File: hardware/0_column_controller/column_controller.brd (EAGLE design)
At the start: 45 parts, among them J3 RJ45, J4 JTAG, J7 RJ45, U1 PCA9615

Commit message: proto schematic for v11 column controller
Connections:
- new net RXI: U$13.PA11
- new net TXO: U$13.PA10
- net 5V: now also J3.4, J7.4
- net GND: now also J3.5, J7.5
- net LED0: now also U$13.PA02; no longer U$13.PA10
- net LED1: now also U$13.PA04; no longer U$13.PA11
- net LED2: now also U$13.PA06; no longer U$13.PA14
- net LED3: now also U$13.PA07; no longer U$13.PA15
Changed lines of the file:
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@@
 <contactref element="J1" pad="2"/>
 <contactref element="J1" pad="1"/>
+<contactref element="J3" pad="5"/>
+<contactref element="J7" pad="5"/>
+<wire x1="113.03" y1="106.045" x2="115.57" y2="104.775" width="0" layer="19" extent="1-1"/>
 <wire x1="109.22" y1="102.235" x2="113.03" y2="106.045" width="0" layer="19" extent="1-1"/>
-<wire x1="83.4" y1="106.68" x2="109.22" y2="102.235" width="0" layer="19" extent="1-1"/>
+<wire x1="106.68" y1="103.505" x2="109.22" y2="102.235" width="0" layer="19" extent="1-1"/>
+<wire x1="83.4" y1="106.68" x2="106.68" y2="103.505" width="0" layer="19" extent="1-1"/>
 <wire x1="83.4" y1="107.95" x2="83.4" y2="106.68" width="0" layer="19" extent="1-1"/>
 <wire x1="83.4" y1="109.22" x2="83.4" y2="107.95" width="0" layer="19" extent="1-1"/>
@@
 <contactref element="J1" pad="3"/>
 <contactref element="J1" pad="4"/>
-<wire x1="106.68" y1="106.045" x2="115.57" y2="102.235" width="0" layer="19" extent="1-1"/>
+<contactref element="J3" pad="4"/>
+<contactref element="J7" pad="4"/>
+<wire x1="113.03" y1="103.505" x2="115.57" y2="102.235" width="0" layer="19" extent="1-1"/>
+<wire x1="109.22" y1="104.775" x2="113.03" y2="103.505" width="0" layer="19" extent="1-1"/>
+<wire x1="106.68" y1="106.045" x2="109.22" y2="104.775" width="0" layer="19" extent="1-1"/>
 <wire x1="114.085" y1="72.7075" x2="115.57" y2="102.235" width="0" layer="19" extent="1-1"/>
 <wire x1="114.085" y1="71.12" x2="114.085" y2="72.7075" width="0" layer="19" extent="1-1"/>
@@
 <signal name="LED0">
 <contactref element="R6" pad="1"/>
-<contactref element="U$13" pad="PA10"/>
-<wire x1="21.59" y1="106.68" x2="105.83" y2="59.69" width="0" layer="19" extent="1-1"/>
+<contactref element="U$13" pad="PA02"/>
+<wire x1="36.83" y1="88.9" x2="105.83" y2="59.69" width="0" layer="19" extent="1-1"/>
 </signal>
 <signal name="LED1">
 <contactref element="R7" pad="1"/>
-<contactref element="U$13" pad="PA11"/>
-<wire x1="21.59" y1="104.14" x2="105.83" y2="58.42" width="0" layer="19" extent="1-1"/>
+<contactref element="U$13" pad="PA04"/>
+<wire x1="36.83" y1="96.52" x2="105.83" y2="58.42" width="0" layer="19" extent="1-1"/>
 </signal>
 <signal name="LED2">
 <contactref element="R8" pad="1"/>
-<contactref element="U$13" pad="PA14"/>
-<wire x1="21.59" y1="96.52" x2="105.83" y2="57.15" width="0" layer="19" extent="1-1"/>
+<contactref element="U$13" pad="PA06"/>
+<wire x1="21.59" y1="81.28" x2="105.83" y2="57.15" width="0" layer="19" extent="1-1"/>
 </signal>
 <signal name="LED3">
 <contactref element="R9" pad="1"/>
-<contactref element="U$13" pad="PA15"/>
-<wire x1="21.59" y1="88.9" x2="105.83" y2="55.88" width="0" layer="19" extent="1-1"/>
+<contactref element="U$13" pad="PA07"/>
+<wire x1="21.59" y1="78.74" x2="105.83" y2="55.88" width="0" layer="19" extent="1-1"/>
 </signal>
 <signal name="B0">
@@
 <wire x1="41.0972" y1="93.98" x2="36.83" y2="93.98" width="0" layer="19" extent="1-1"/>
 </signal>
+<signal name="TXO">
+<contactref element="U$13" pad="PA10"/>
+</signal>
+<signal name="RXI">
+<contactref element="U$13" pad="PA11"/>
+</signal>
 </signals>

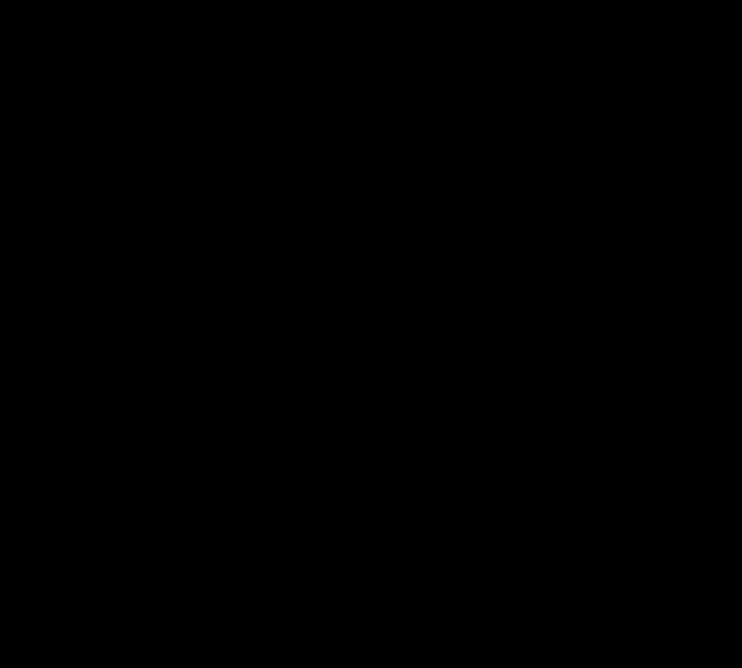
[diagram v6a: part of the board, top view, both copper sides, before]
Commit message: add uart / i2c / column debug access headers
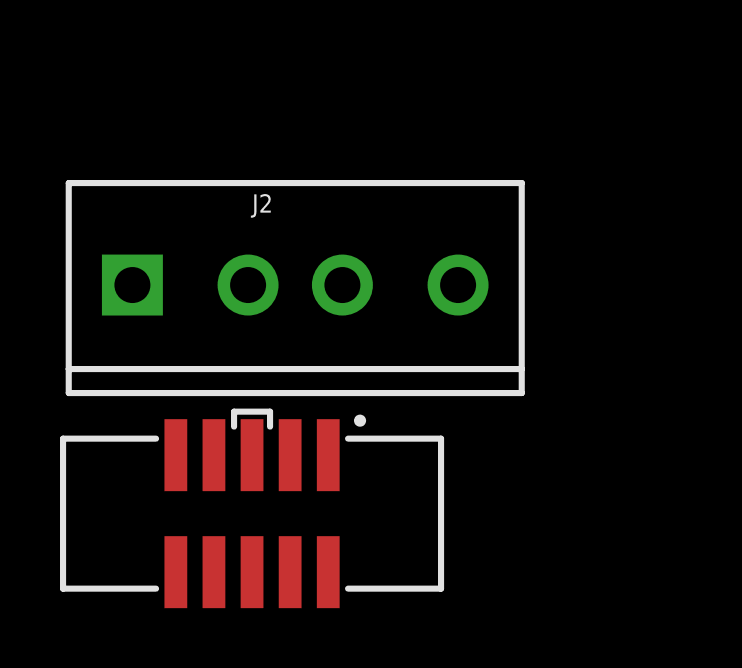
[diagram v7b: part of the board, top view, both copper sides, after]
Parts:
- added J2: (no value), SparkFun-Connectors:SCREWTERMINAL-3.5MM-4_LOCK
- added J5: JTAG, SparkFun-Connectors:2X5-SMD-1.27MM
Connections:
- net 5V: now also J5.4, J5.5, J5.7, J5.9
- net DOUT: now also J5.6
- net GND: now also J5.1, J5.2, J5.3
- net RXI: now also J2.4
- net SCL_COLUMN: now also J5.10
- net SCL_NETWORK: now also J2.1
- net SDA_COLUMN: now also J5.8
- net SDA_NETWORK: now also J2.2
- net TXO: now also J2.3
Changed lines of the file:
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@@
 <attribute name="VALUE" x="41.5036" y="92.837" size="0.6096" layer="27" font="vector" ratio="20" align="top-center"/>
+</element>
+<element name="J2" library="SparkFun-Connectors" package="SCREWTERMINAL-3.5MM-4_LOCK" value="" x="-5.08" y="-15.24">
+<attribute name="NAME" x="-1.27" y="-12.827" size="0.6096" layer="25" font="vector" ratio="20"/>
+<attribute name="VALUE" x="-1.27" y="-13.716" size="0.6096" layer="27" font="vector" ratio="20"/>
+</element>
+<element name="J5" library="SparkFun-Connectors" package="2X5-SMD-1.27MM" value="JTAG" x="-1.27" y="-22.86">
+<attribute name="PROD_ID" value="CONN-14503" x="-1.27" y="-22.86" size="1.778" layer="27" font="vector" ratio="15" display="off"/>
 </element>
 </elements>
@@
 <contactref element="J3" pad="5"/>
 <contactref element="J7" pad="5"/>
+<contactref element="J5" pad="1"/>
+<contactref element="J5" pad="3"/>
+<contactref element="J5" pad="2"/>
 <wire x1="113.03" y1="106.045" x2="115.57" y2="104.775" width="0" layer="19" extent="1-1"/>
 <wire x1="109.22" y1="102.235" x2="113.03" y2="106.045" width="0" layer="19" extent="1-1"/>
@@
 <wire x1="36.83" y1="104.14" x2="79.021" y2="112.0425" width="0" layer="19" extent="1-1"/>
 <wire x1="21.59" y1="99.06" x2="36.83" y2="104.14" width="0" layer="19" extent="1-1"/>
+<wire x1="1.27" y1="-20.91" x2="69.3293" y2="63.5" width="0" layer="19" extent="1-1"/>
+<wire x1="0" y1="-20.91" x2="1.27" y2="-20.91" width="0" layer="19" extent="1-1"/>
+<wire x1="1.27" y1="-24.81" x2="1.27" y2="-20.91" width="0" layer="19" extent="1-1"/>
 </signal>
 <signal name="SCL_COLUMN">
@@
 <contactref element="J4" pad="10"/>
 <contactref element="U$13" pad="PA09"/>
+<contactref element="J5" pad="10"/>
 <wire x1="56.3" y1="27.305" x2="106.09" y2="69.85" width="0" layer="19" extent="1-1"/>
 <wire x1="21.59" y1="93.98" x2="56.3" y2="27.305" width="0" layer="19" extent="1-1"/>
+<wire x1="-3.81" y1="-24.81" x2="56.3" y2="27.305" width="0" layer="19" extent="1-1"/>
 </signal>
 <signal name="SDA_COLUMN">
@@
 <contactref element="J4" pad="8"/>
 <contactref element="U$13" pad="PA08"/>
+<contactref element="J5" pad="8"/>
 <wire x1="56.3" y1="28.8925" x2="106.09" y2="71.12" width="0" layer="19" extent="1-1"/>
 <wire x1="21.59" y1="91.44" x2="56.3" y2="28.8925" width="0" layer="19" extent="1-1"/>
+<wire x1="-2.54" y1="-24.81" x2="56.3" y2="28.8925" width="0" layer="19" extent="1-1"/>
 </signal>
 <signal name="DOUT">
@@
 <contactref element="R5" pad="2"/>
 <contactref element="JP1" pad="2"/>
+<contactref element="J5" pad="6"/>
 <wire x1="86.8807" y1="44.45" x2="106.09" y2="72.39" width="0" layer="19" extent="1-1"/>
 <wire x1="87.21" y1="41.91" x2="86.8807" y2="44.45" width="0" layer="19" extent="1-1"/>
+<wire x1="-1.27" y1="-24.81" x2="87.21" y2="41.91" width="0" layer="19" extent="1-1"/>
 </signal>
 <signal name="5V">
@@
 <contactref element="J3" pad="4"/>
 <contactref element="J7" pad="4"/>
+<contactref element="J5" pad="9"/>
+<contactref element="J5" pad="7"/>
+<contactref element="J5" pad="5"/>
+<contactref element="J5" pad="4"/>
 <wire x1="113.03" y1="103.505" x2="115.57" y2="102.235" width="0" layer="19" extent="1-1"/>
 <wire x1="109.22" y1="104.775" x2="113.03" y2="103.505" width="0" layer="19" extent="1-1"/>
@@
 <wire x1="36.83" y1="106.68" x2="106.68" y2="106.045" width="0" layer="19" extent="1-1"/>
 <wire x1="36.83" y1="101.6" x2="36.83" y2="106.68" width="0" layer="19" extent="1-1"/>
+<wire x1="-1.27" y1="-20.91" x2="113.5022" y2="20.32" width="0" layer="19" extent="1-1"/>
+<wire x1="-2.54" y1="-20.91" x2="-1.27" y2="-20.91" width="0" layer="19" extent="1-1"/>
+<wire x1="-3.81" y1="-20.91" x2="-2.54" y2="-20.91" width="0" layer="19" extent="1-1"/>
+<wire x1="0" y1="-24.81" x2="-1.27" y2="-20.91" width="0" layer="19" extent="1-1"/>
 </signal>
 <signal name="SCL_NETWORK">
@@
 <contactref element="R1" pad="1"/>
 <contactref element="U1" pad="4"/>
+<contactref element="J2" pad="1"/>
 <wire x1="36.83" y1="86.36" x2="79.021" y2="112.5475" width="0" layer="19" extent="1-1"/>
 <wire x1="56.3" y1="8.89" x2="36.83" y2="86.36" width="0" layer="19" extent="1-1"/>
+<wire x1="-5.2578" y1="-15.24" x2="56.3" y2="8.89" width="0" layer="19" extent="1-1"/>
 </signal>
 <signal name="SDA_NETWORK">
@@
 <contactref element="R4" pad="1"/>
 <contactref element="U1" pad="2"/>
+<contactref element="J2" pad="2"/>
 <wire x1="36.83" y1="81.28" x2="79.021" y2="113.5475" width="0" layer="19" extent="1-1"/>
 <wire x1="56.3" y1="10.16" x2="36.83" y2="81.28" width="0" layer="19" extent="1-1"/>
+<wire x1="-1.4022" y1="-15.24" x2="56.3" y2="10.16" width="0" layer="19" extent="1-1"/>
 </signal>
 <signal name="N$1">
@@
 <signal name="TXO">
 <contactref element="U$13" pad="PA10"/>
+<contactref element="J2" pad="3"/>
+<wire x1="1.7422" y1="-15.24" x2="21.59" y2="106.68" width="0" layer="19" extent="1-1"/>
 </signal>
 <signal name="RXI">
 <contactref element="U$13" pad="PA11"/>
+<contactref element="J2" pad="4"/>
+<wire x1="5.5978" y1="-15.24" x2="21.59" y2="104.14" width="0" layer="19" extent="1-1"/>
 </signal>
 </signals>

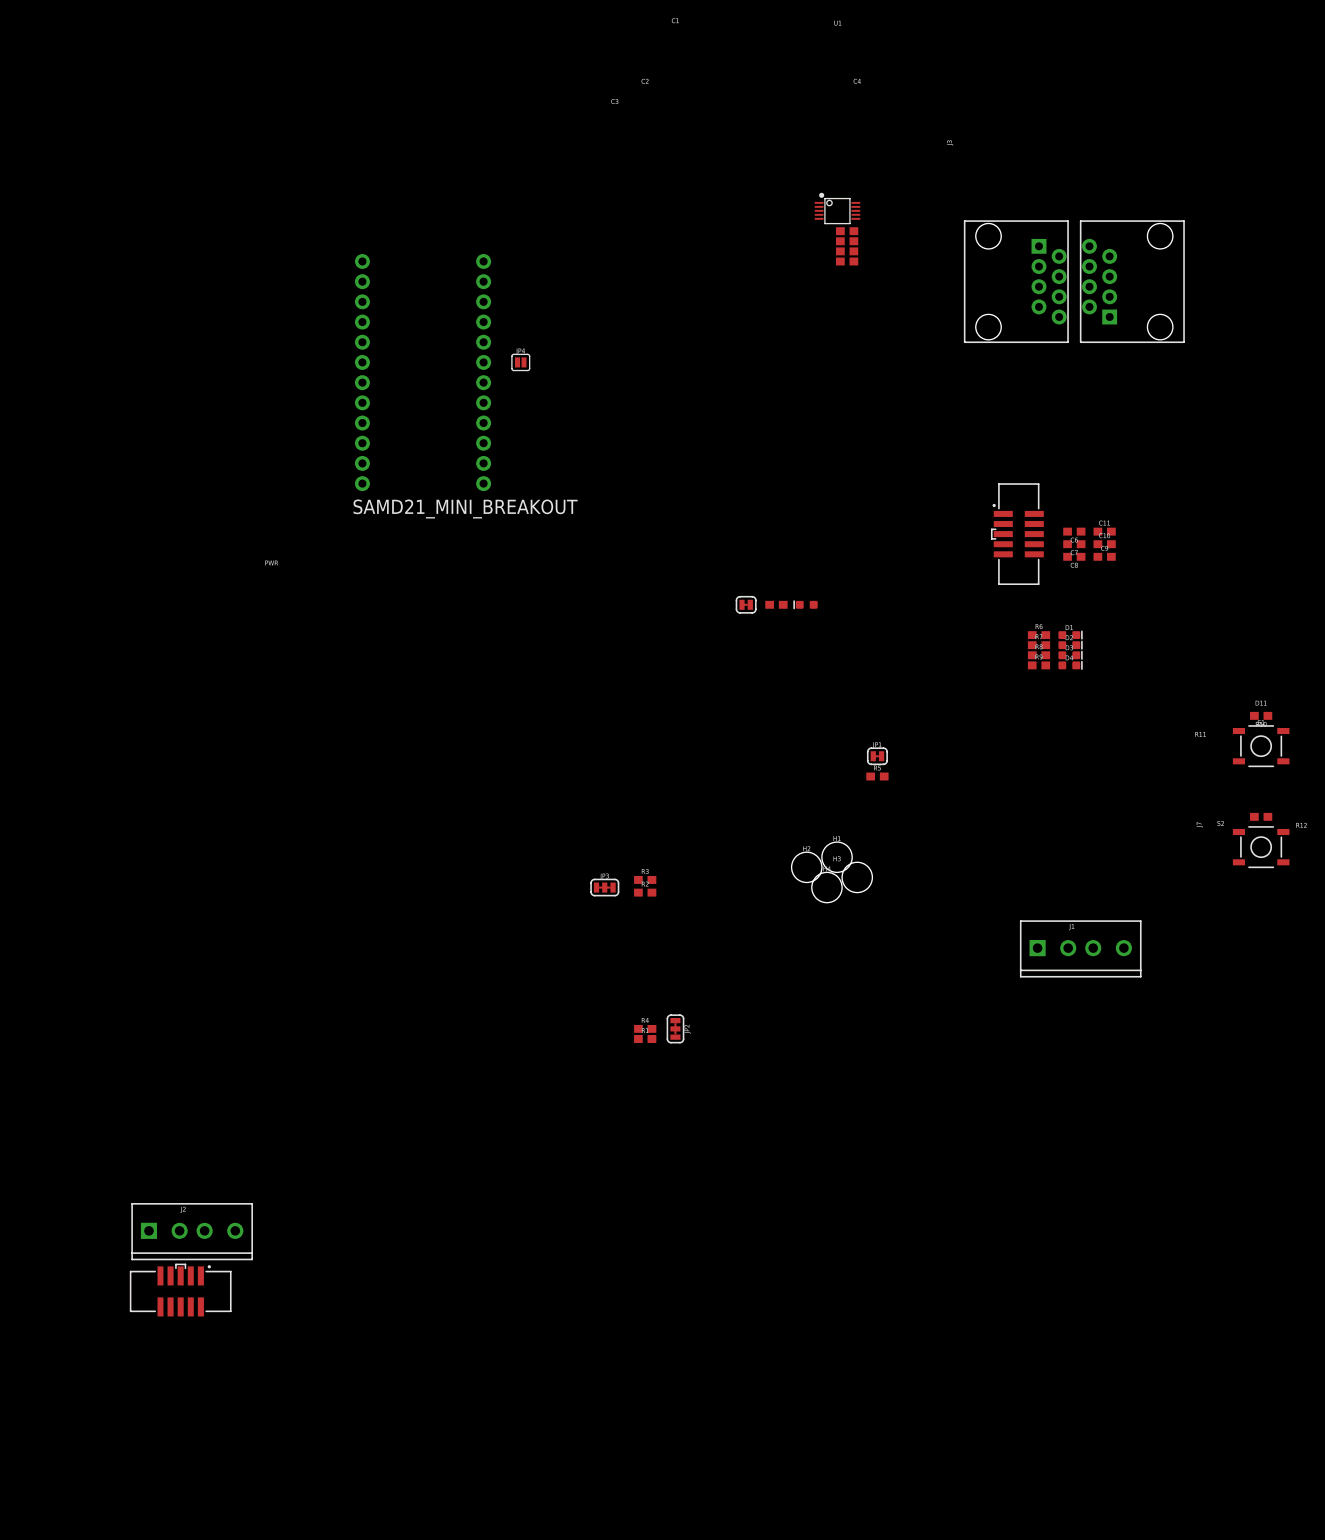
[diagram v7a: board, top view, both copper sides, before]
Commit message: redesign + order column_controller board
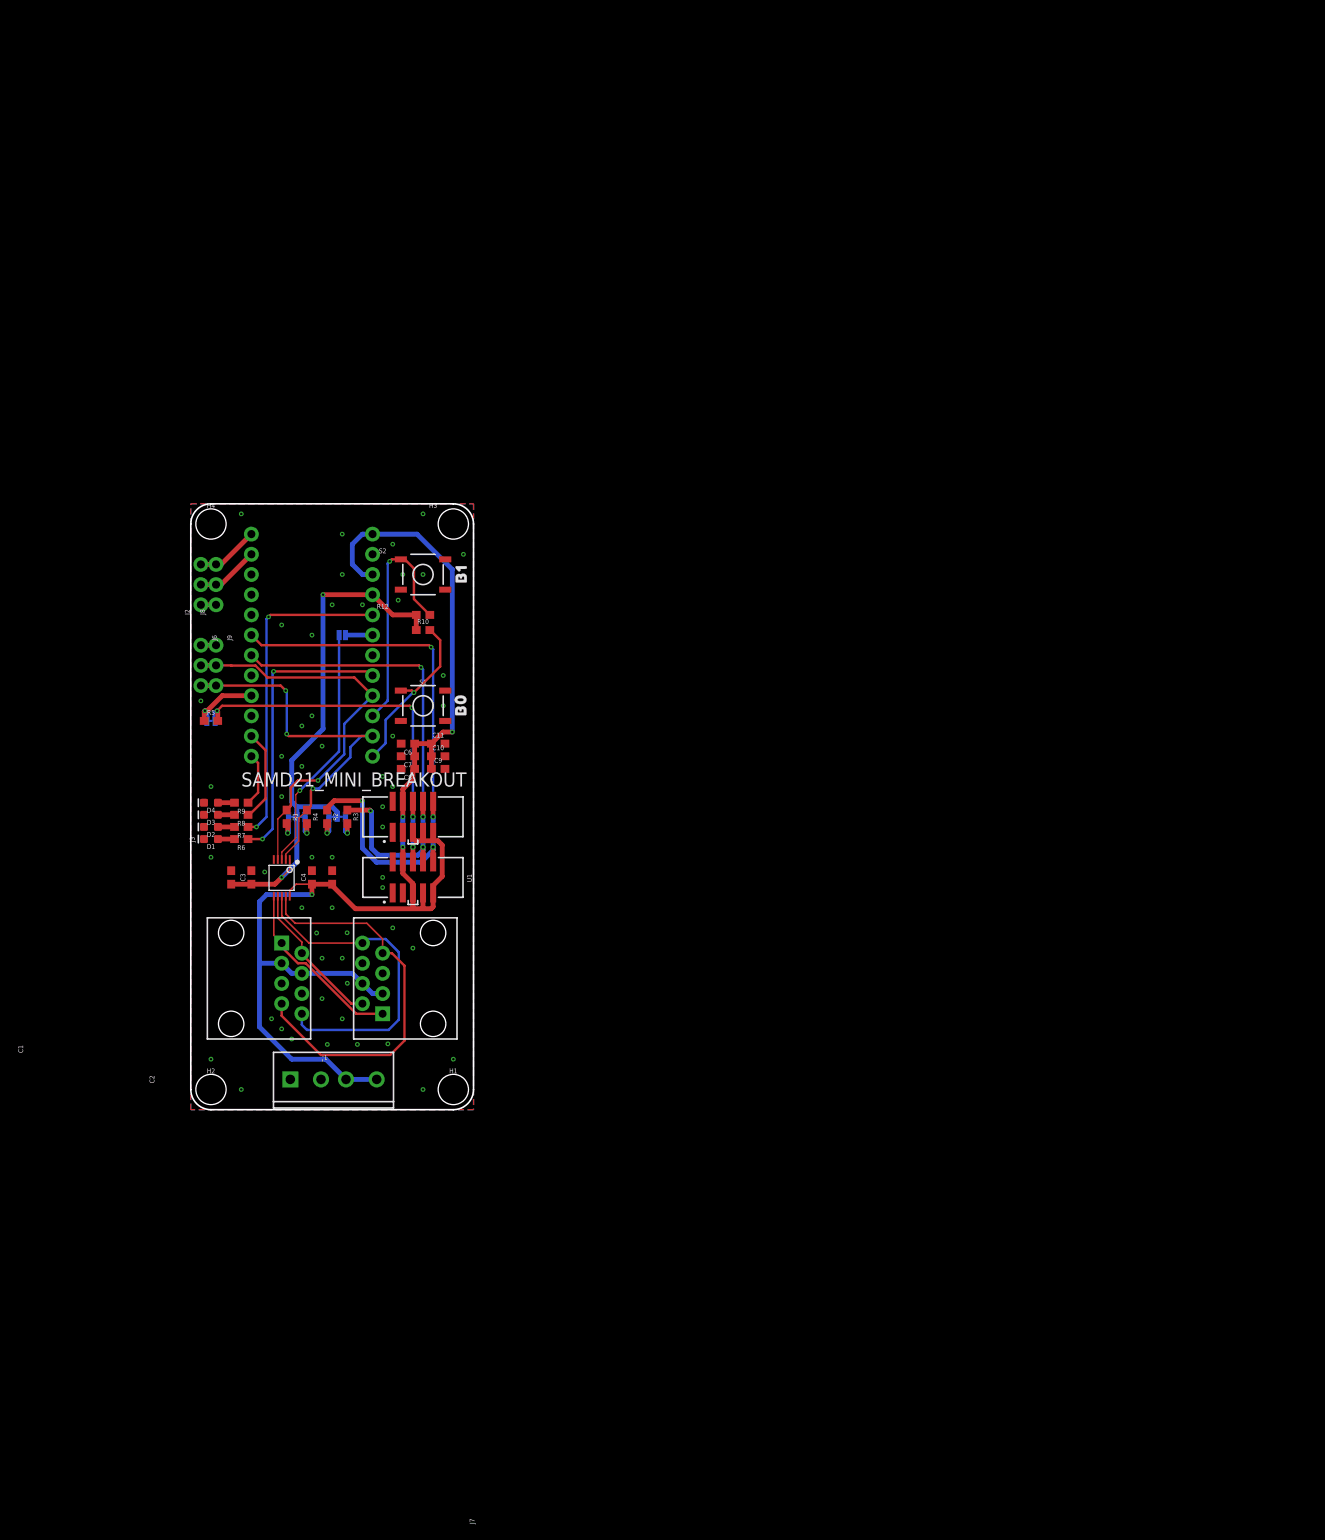
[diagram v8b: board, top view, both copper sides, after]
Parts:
- removed D11: RED, SparkFun-LED:LED-0603
- removed PWR: JUMPER-SMT_2_NC_TRACE_SILK, SparkFun-Jumpers:SMT-JUMPER_2_NC_TRACE_SILK
- removed R11: 1k, SparkFun-Resistors:0603
- added J6, J8, J9: (no value), SparkFun-Connectors:1X03_NO_SILK
- added U$1: (no value), buzzard_labels:OCLYKE#DEV7
- added U$10: (no value), buzzard_labels:NETWORK_SDA7
- added U$11: (no value), buzzard_labels:NETWORK_SCL6
- added U$12: (no value), buzzard_labels:TXO4
- added U$14: (no value), buzzard_labels:RXI5
- added U$2: (no value), buzzard_labels:B00
- added U$3: (no value), buzzard_labels:B11
- added U$4: (no value), buzzard_labels:5V2
- added U$5: (no value), buzzard_labels:#GND#6
- added U$6: (no value), buzzard_labels:PCA_EN2
- added U$7: (no value), buzzard_labels:DOUT_BYP3
- added U$8: (no value), buzzard_labels:COLUMN_I2C4
- added U$9: (no value), buzzard_labels:NETWORK_I2C4
- J2: device SparkFun-Connectors:SCREWTERMINAL-3.5MM-4_LOCK -> SparkFun-Connectors:1X03_NO_SILK
- moved J3 129.4 mm to (5.08, 16.5)
- moved J7 126.7 mm to (30.5, 16.5)
- moved C1 112.3 mm to (5.08, 29.2), turned to 90 degrees
- moved D1 111.0 mm to (2.54, 34.0), turned to 180 degrees
- moved S2 110.8 mm to (29.2, 67.3)
- moved D2 110.3 mm to (2.54, 35.6), turned to 180 degrees
- moved D3 109.8 mm to (2.54, 37.1), turned to 180 degrees
- moved D4 109.3 mm to (2.54, 38.6), turned to 180 degrees
- moved U1 109.1 mm to (11.4, 29.2), turned to 270 degrees
- moved C3 108.7 mm to (7.62, 29.2), turned to 90 degrees
- moved R12 108.4 mm to (29.2, 62.2), turned to 0 degrees
- moved R10 106.0 mm to (29.2, 60.3), turned to 0 degrees
- moved S1 105.5 mm to (29.2, 50.8)
- moved C4 104.6 mm to (15.2, 29.2), turned to 90 degrees
- moved R6 103.6 mm to (6.35, 34.0), turned to 180 degrees
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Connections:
- removed net N$13: D11.C, R11.1
- removed net N$14: PWR.2, R11.2
- net 3.3V: no longer C2.1, C4.1, D11.A, U1.10
- net 5V: now also C2.1, C4.1, U1.10
- net GND: now also J2.1, J6.1, J8.1, J9.1; no longer PWR.1
- net RXI: now also J2.2, J8.2; no longer J2.4
- net SCL_NETWORK: now also J6.2, J9.2; no longer J2.1
- net SDA_NETWORK: now also J6.3, J9.3; no longer J2.2
- net TXO: now also J8.3
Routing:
- net 5V: track 0.00 -> 167.7 mm, vias 0 -> 4
- net SCL_COLUMN: track 0.00 -> 74.0 mm, vias 0 -> 4
- net 3.3V: track 0.00 -> 68.3 mm, vias 0 -> 2
- net SDA_COLUMN: track 0.00 -> 63.7 mm, vias 0 -> 4
- net SCL_NETWORK: track 0.00 -> 50.2 mm, vias 0 -> 1
- net DSDA_N: track 0.00 -> 50.1 mm
- net DOUT: track 0.00 -> 48.9 mm, vias 0 -> 4
- net SDA_NETWORK: track 0.00 -> 48.7 mm, vias 0 -> 3
- net DSDA_P: track 0.00 -> 42.4 mm
- net LED1: track 0.00 -> 41.3 mm, vias 0 -> 2
- net LED0: track 0.00 -> 36.2 mm, vias 0 -> 2
- net PCA_EN: track 0.00 -> 31.2 mm, vias 0 -> 1
- net B1: track 0.00 -> 30.6 mm, vias 0 -> 1
- net DSCL_N: track 0.00 -> 23.0 mm
- net B0: track 0.00 -> 21.8 mm, vias 0 -> 1
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- added copper zone on layer 1, net GND
- added copper zone on layer 16, net GND
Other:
- board outline added: 35.6 x 76.2 mm
